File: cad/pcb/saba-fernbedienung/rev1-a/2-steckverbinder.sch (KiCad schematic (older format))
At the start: 29 parts, among them J301 Conn_01x04, J302 Conn_01x04, J303 Micro_SD_Card, J304 Conn_01x04, J305 AudioJack3, J306 Conn_01x02, J307 Conn_01x04, J308 Conn_01x01, J309 Conn_01x01, J310 Conn_01x01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

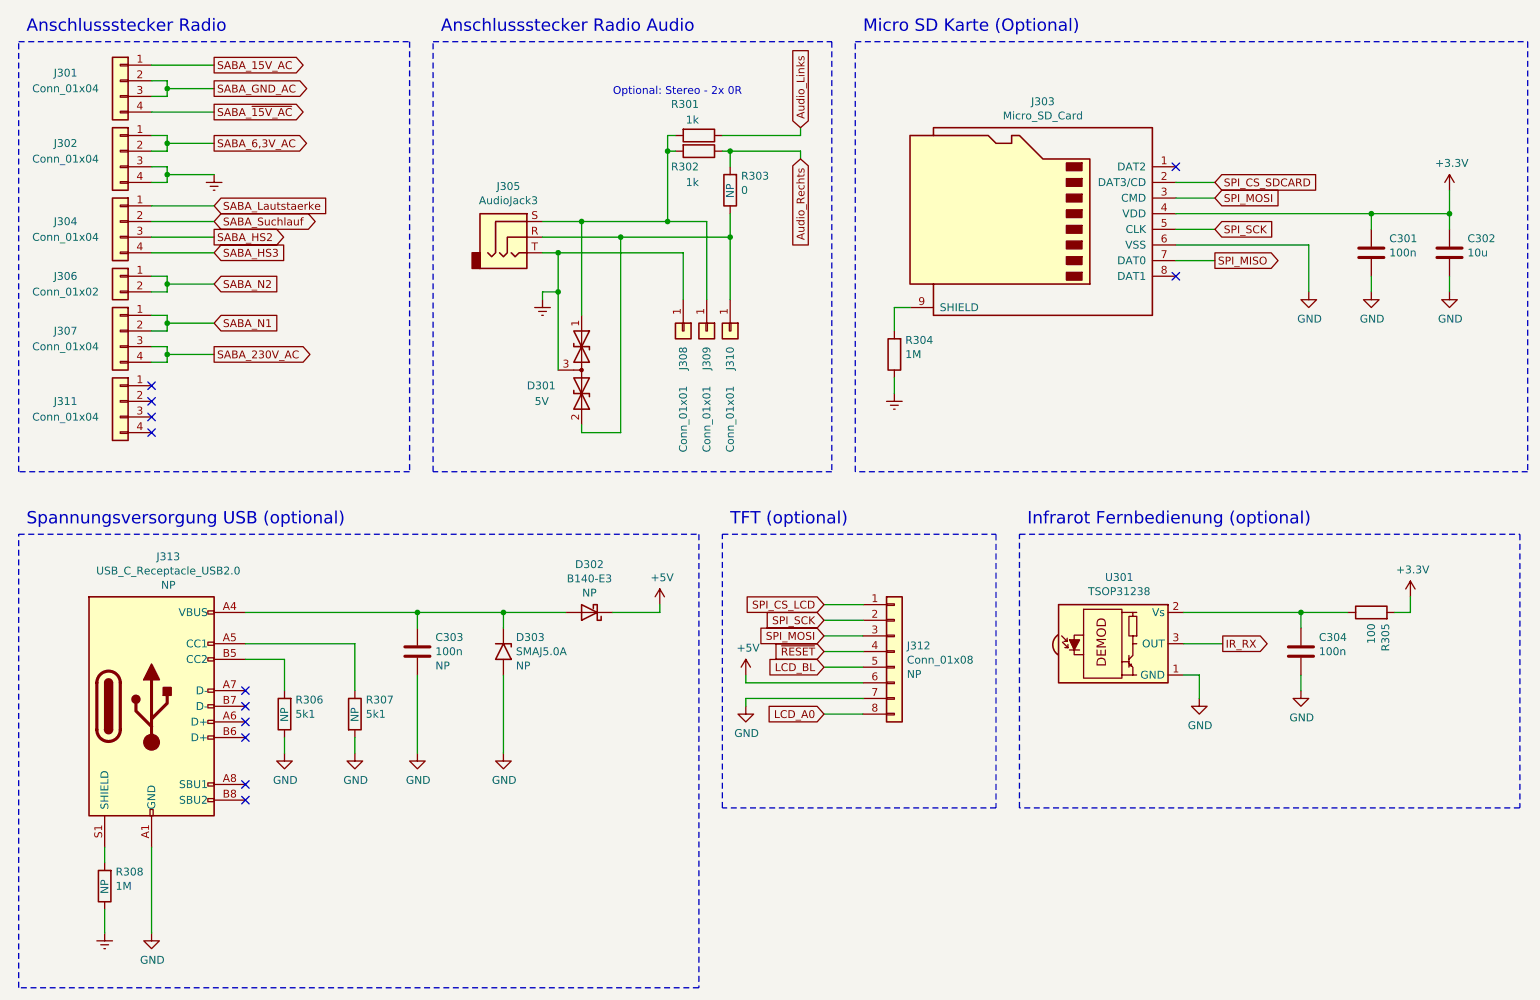
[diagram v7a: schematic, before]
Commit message: PCB: Alle Leitungen verlegt
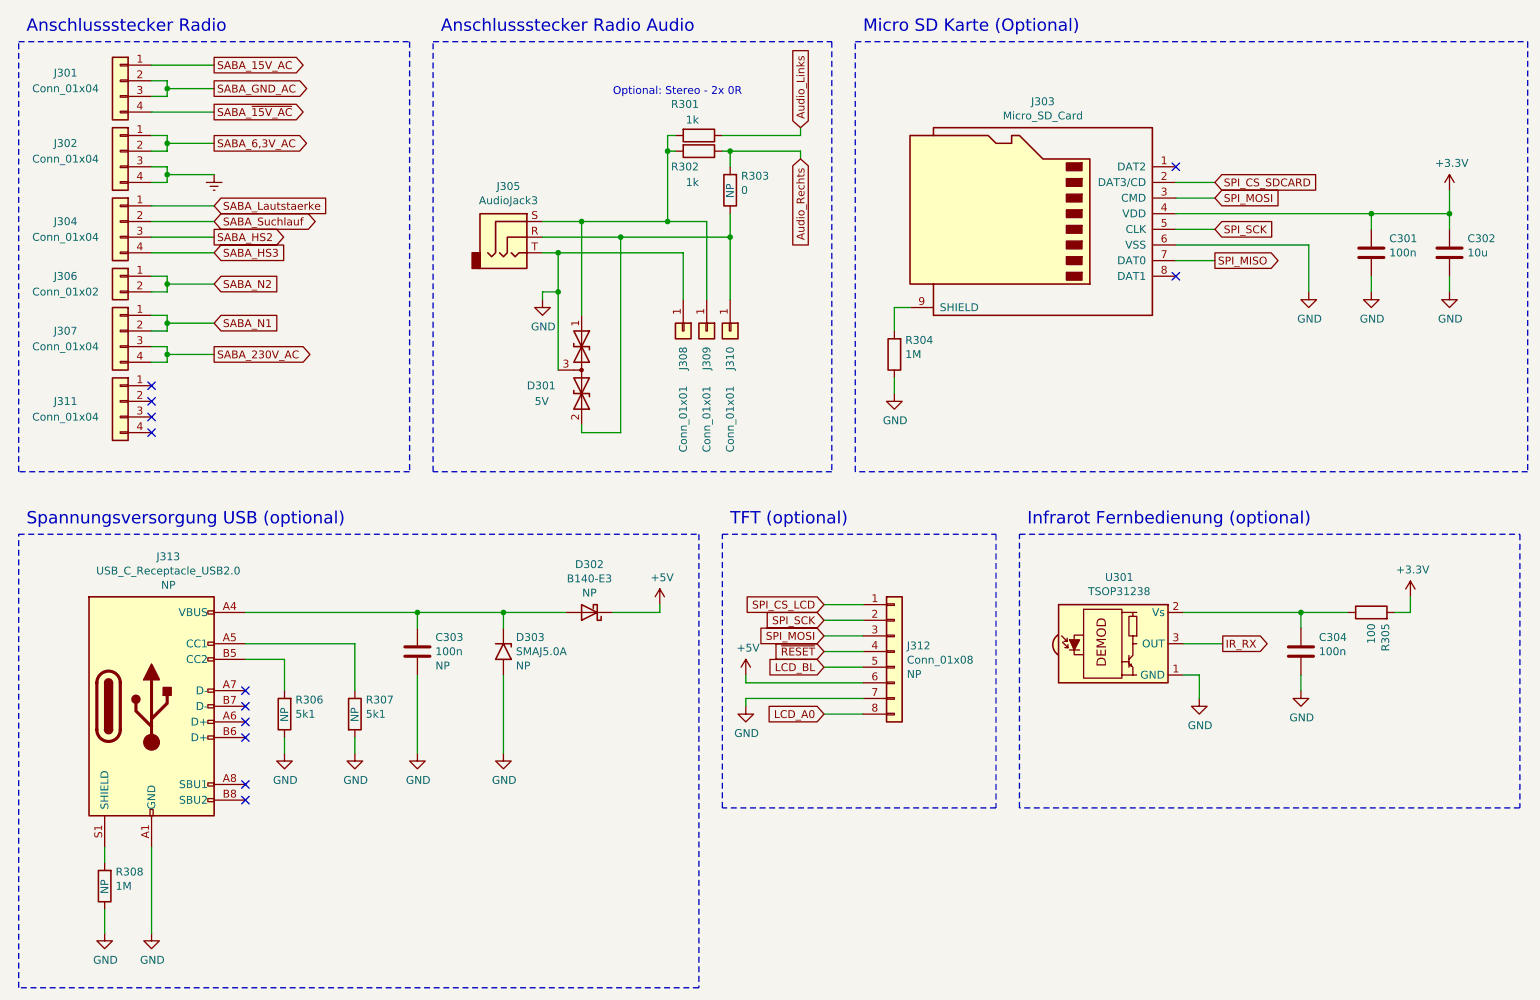
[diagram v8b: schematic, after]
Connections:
- net Earth: no longer D301.3 (common), J305.T, J308.1 (Pin_1), R304.1, R308.1
- net GND: now also D301.3 (common), J305.T, J308.1 (Pin_1), R304.1, R308.1
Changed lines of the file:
@@
-	1    0    0    -1
-$EndComp
-$Comp
-L power:Earth #PWR0307
-U 1 1 600ADE98
-P 6600 3250
-F 0 "#PWR0307" H 6600 3000 50  0001 C CNN
-F 1 "Earth" H 6600 3100 50  0001 C CNN
-F 2 "" H 6600 3250 50  0001 C CNN
-F 3 "~" H 6600 3250 50  0001 C CNN
-	1    6600 3250
-	1    0    0    -1
-$EndComp
-$Comp
-L power:Earth #PWR0318
-U 1 1 600AE860
-P 1550 6700
-F 0 "#PWR0318" H 1550 6450 50  0001 C CNN
-F 1 "Earth" H 1550 6550 50  0001 C CNN
-F 2 "" H 1550 6700 50  0001 C CNN
-F 3 "~" H 1550 6700 50  0001 C CNN
-	1    1550 6700
 	1    0    0    -1
 $EndComp
@@
 NoConn ~ 2450 5750
 NoConn ~ 2450 5850
-$Comp
-L power:Earth #PWR0306
-U 1 1 600ACF99
-P 4350 2650
-F 0 "#PWR0306" H 4350 2400 50  0001 C CNN
-F 1 "Earth" H 4350 2500 50  0001 C CNN
-F 2 "" H 4350 2650 50  0001 C CNN
-F 3 "~" H 4350 2650 50  0001 C CNN
-	1    4350 2650
-	1    0    0    -1
-$EndComp
 Wire Wire Line
 	4350 2600 4350 2650
@@
 $EndComp
 NoConn ~ 1850 3200
+$Comp
+L power:GND #PWR0101
+U 1 1 6003FF39
+P 6600 3250
+F 0 "#PWR0101" H 6600 3000 50  0001 C CNN
+F 1 "GND" H 6605 3077 50  0000 C CNN
+F 2 "" H 6600 3250 50  0001 C CNN
+F 3 "" H 6600 3250 50  0001 C CNN
+	1    6600 3250
+	1    0    0    -1
+$EndComp
+$Comp
+L power:GND #PWR0102
+U 1 1 60040609
+P 4350 2650
+F 0 "#PWR0102" H 4350 2400 50  0001 C CNN
+F 1 "GND" H 4355 2477 50  0000 C CNN
+F 2 "" H 4350 2650 50  0001 C CNN
+F 3 "" H 4350 2650 50  0001 C CNN
+	1    4350 2650
+	1    0    0    -1
+$EndComp
+$Comp
+L power:GND #PWR0103
+U 1 1 60040E02
+P 1550 6700
+F 0 "#PWR0103" H 1550 6450 50  0001 C CNN
+F 1 "GND" H 1555 6527 50  0000 C CNN
+F 2 "" H 1550 6700 50  0001 C CNN
+F 3 "" H 1550 6700 50  0001 C CNN
+	1    1550 6700
+	1    0    0    -1
+$EndComp
 $EndSCHEMATC
